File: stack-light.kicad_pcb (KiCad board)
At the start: 2 copper layers, 82 x 56.5 mm, 129 parts, among them J2 Mini-DIN-6, J3 Barrel_Jack_Switch, J4 USB_C_Receptacle_USB2.0, Q1 2N7002, Q2 2N7002, Q3 2N7002, Q4 2N7002, Q5 2N7002, Q6 BC817-40, Q7 BC817-40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

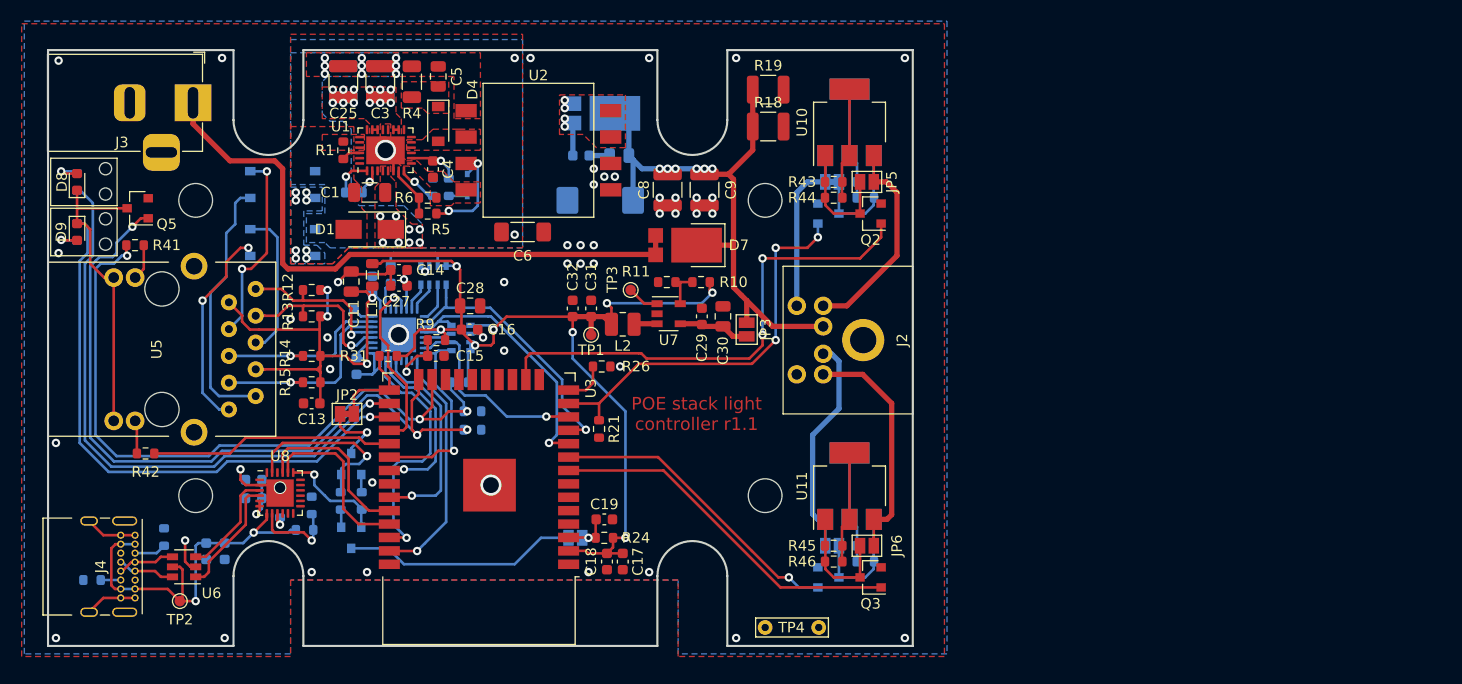
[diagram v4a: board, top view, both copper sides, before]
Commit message: Reduce case screw notch size and placement to better match case
Also center the mini-din output connector
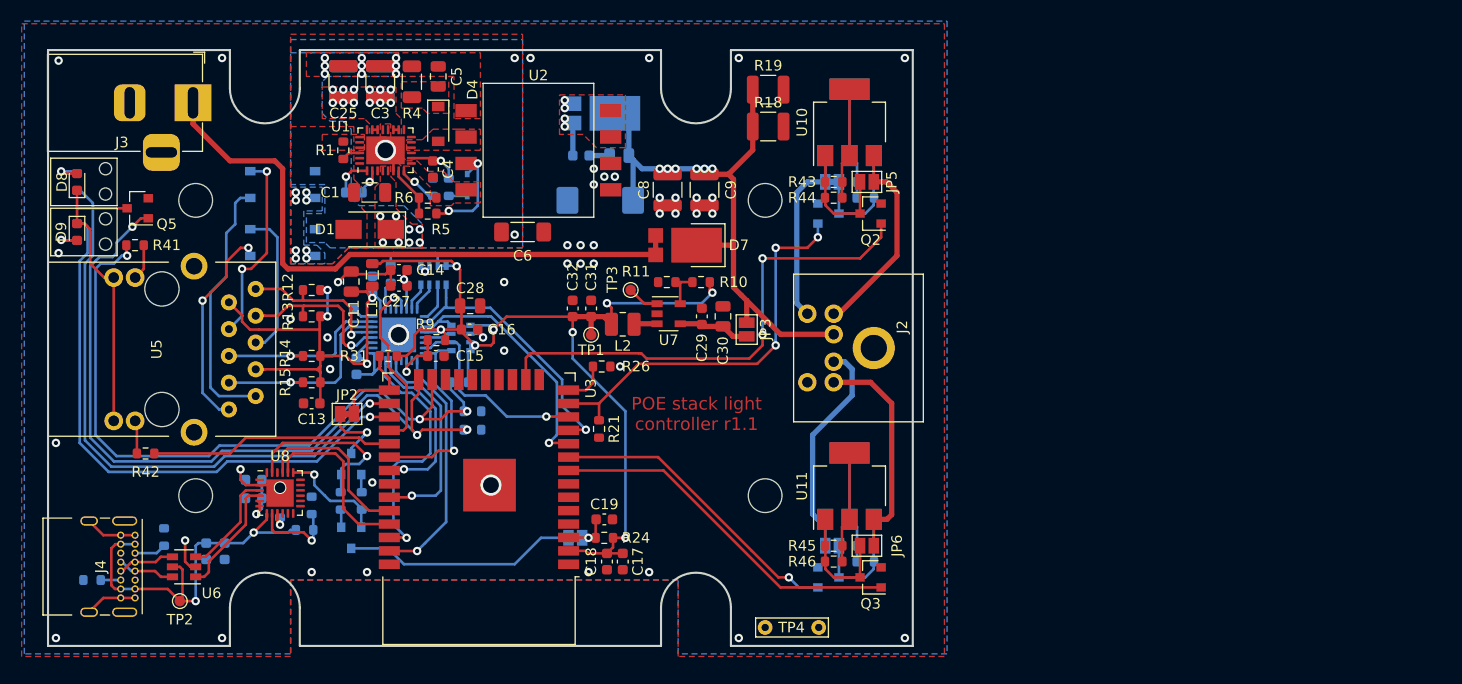
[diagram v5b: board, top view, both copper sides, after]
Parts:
- moved J2 1.25 mm to (183.0, 78.2)
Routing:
- net /Output/Drive_Green: track 22.6 -> 21.3 mm
- net +12V: track 57.1 -> 58.4 mm
- net /Output/Drive_Buzzer: track 16.4 -> 17.5 mm
- net /Output/Drive_Yellow: track 20.1 -> 19.4 mm
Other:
- outline, holes or cut-outs redrawn

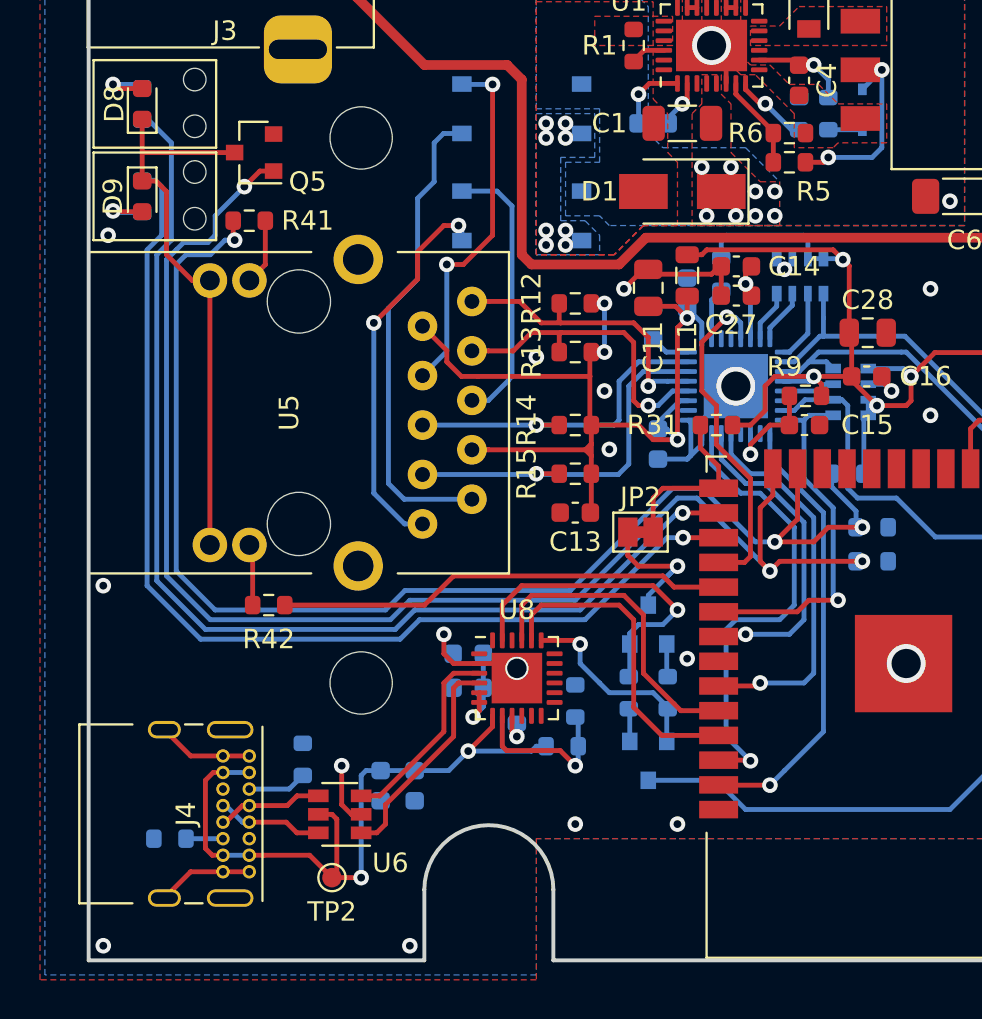
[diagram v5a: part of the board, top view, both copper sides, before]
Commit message: Adjust front IO to work with a flush panel
also removed the LED enable transistor
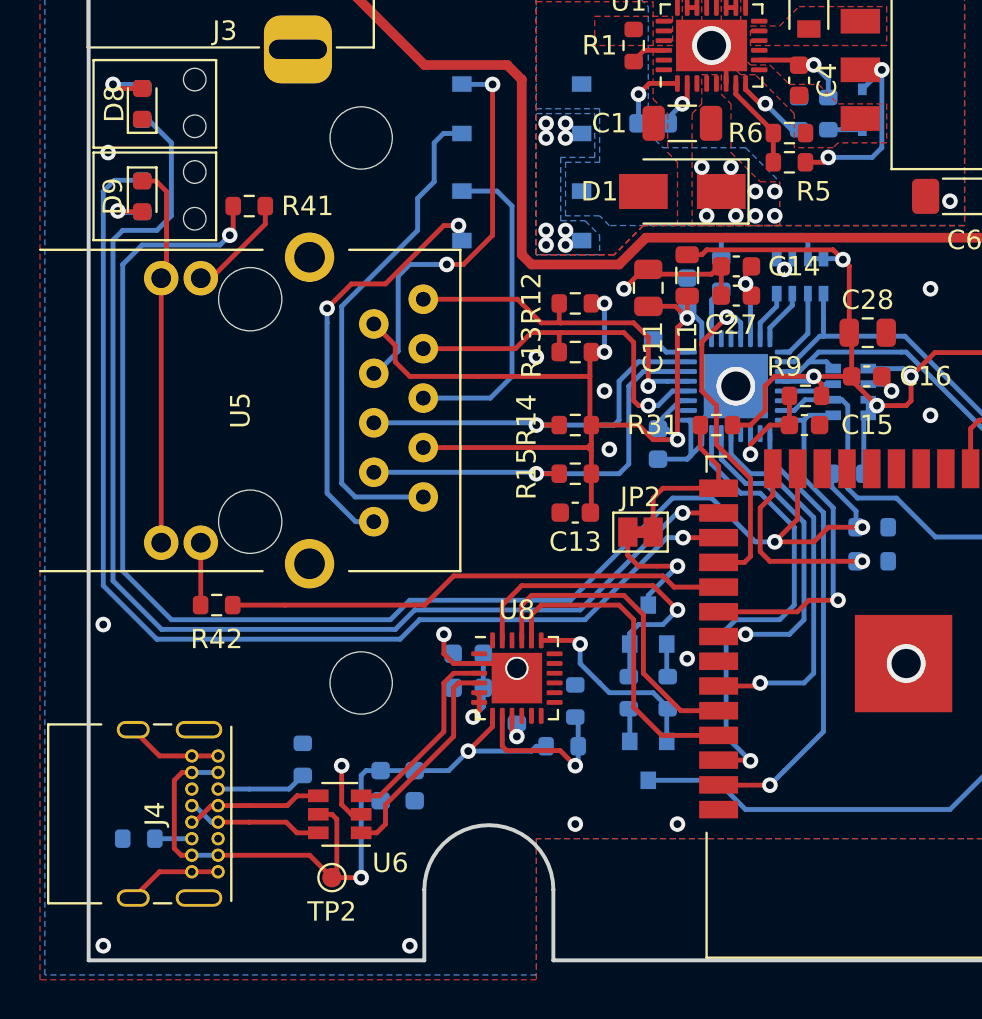
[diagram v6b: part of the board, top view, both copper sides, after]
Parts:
- removed Q5: 2N7002, Package_TO_SOT_SMD:SOT-23
- moved R42 2.67 mm to (106.6, 88.2)
- moved U5 2.50 mm to (108.3, 78.2)
- moved J4 1.60 mm to (106.7, 96.0)
- moved R39 1.60 mm to (102.6, 100.2)
- moved R41 0.75 mm to (108.2, 67.8)
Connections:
- net LED_EN renamed Net-(R25-Pad1)
- D8 pad 1: LED_GND -> GND
- D9 pad 1: LED_GND -> GND
- U5 pad 12: LED_GND -> GND
- U5 pad 14: LED_GND -> GND
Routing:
- net Net-(R25-Pad1): track 71.3 -> 10.3 mm, vias 3 -> 1
- net LED_GND: track 29.0 -> 0.00 mm
- net GND: track 37.2 -> 56.8 mm
- net LED_status: track 68.2 -> 74.1 mm
- net Net-(C11-Pad2): track 49.4 -> 54.4 mm
- net LED_LOCATE: track 57.2 -> 61.4 mm
- net LED_ARTNET: track 54.6 -> 57.4 mm
- net LED_net: track 23.1 -> 25.8 mm
- net /Ethernet Controller/TDP: track 15.5 -> 18.1 mm
- net /Ethernet Controller/RDP: track 17.4 -> 19.9 mm
- net /Ethernet Controller/RDN: track 19.4 -> 21.9 mm
- net /Ethernet Controller/TDN: track 16.2 -> 18.6 mm
- net POE_V2+: track 14.2 -> 16.7 mm
- net POE_V1+: track 18.5 -> 20.7 mm
- net Net-(R41-Pad1): track 3.46 -> 5.39 mm
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
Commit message: Add option for SIL regulator module due to component shortage
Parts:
- added U13: TSR_1-2433, Converter_DCDC:Converter_DCDC_TRACO_TSR-1_THT, F.Cu at (164.2, 80.8)
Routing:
- net +3V3: track 104.2 -> 113.6 mm
- net Yellow: track 47.0 -> 52.9 mm
- net Net-(C29-Pad1): track 6.80 -> 10.7 mm
- net Buzzer: track 38.5 -> 40.4 mm
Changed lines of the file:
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@@
     (thickness 1.6)
     (drawings 22)
-    (tracks 912)
+    (tracks 920)
     (zones 0)
-    (modules 128)
+    (modules 129)
     (nets 130)
   )
@@
     (add_net Yellow)
   )
+  (module Converter_DCDC:Converter_DCDC_TRACO_TSR-1_THT (layer F.Cu)
+    (at 164.25 80.75 180)
+    (descr "DCDC-Converter, TRACO, TSR 1-xxxx")
+    (tags "DCDC-Converter TRACO TSR-1")
+    (fp_text reference U13 (at -1.5 -6.71) (layer F.SilkS)
+      (effects (font (size 1 1) (thickness 0.15)))
+    )
+    (fp_text value TSR_1-2433 (at 2.5 3.25) (layer F.Fab)
+      (effects (font (size 1 1) (thickness 0.15)))
+    )
+    (fp_line (start -3.75 2.45) (end -1.42 2.45) (layer F.SilkS) (width 0.12))
+    (fp_line (start -3.75 0) (end -3.75 2.45) (layer F.SilkS) (width 0.12))
+    (fp_line (start -3.3 1) (end -2.3 2) (layer F.Fab) (width 0.1))
+    (fp_line (start -3.3 1) (end -3.3 -5.6) (layer F.Fab) (width 0.1))
+    (fp_line (start 8.4 2) (end 8.4 -5.6) (layer F.Fab) (width 0.1))
+    (fp_line (start -3.3 -5.6) (end 8.4 -5.6) (layer F.Fab) (width 0.1))
+    (fp_line (start -3.55 2.25) (end -3.55 -5.85) (layer F.CrtYd) (width 0.05))
+    (fp_line (start 8.65 2.25) (end -3.55 2.25) (layer F.CrtYd) (width 0.05))
+    (fp_line (start 8.65 -5.85) (end 8.65 2.25) (layer F.CrtYd) (width 0.05))
+    (fp_line (start -3.55 -5.85) (end 8.65 -5.85) (layer F.CrtYd) (width 0.05))
+    (fp_line (start 8.52 2.12) (end -3.42 2.12) (layer F.SilkS) (width 0.12))
+    (fp_line (start 8.52 -5.73) (end 8.52 2.12) (layer F.SilkS) (width 0.12))
+    (fp_line (start -3.42 -5.73) (end 8.52 -5.73) (layer F.SilkS) (width 0.12))
+    (fp_line (start -3.42 2.12) (end -3.42 -5.73) (layer F.SilkS) (width 0.12))
+    (fp_line (start -2.3 2) (end 8.4 2) (layer F.Fab) (width 0.1))
+    (fp_text user %R (at 3 -3) (layer F.Fab)
+      (effects (font (size 1 1) (thickness 0.15)))
+    )
+    (pad 3 thru_hole oval (at 5.08 0 180) (size 1.5 2.5) (drill 1) (layers *.Cu *.Mask)
+      (net 10 +3V3))
+    (pad 2 thru_hole oval (at 2.54 0 180) (size 1.5 2.5) (drill 1) (layers *.Cu *.Mask)
+      (net 6 GND))
+    (pad 1 thru_hole rect (at 0 0 180) (size 1.5 2.5) (drill 1) (layers *.Cu *.Mask)
+      (net 128 "Net-(C29-Pad1)"))
+    (model ${KISYS3DMOD}/Converter_DCDC.3dshapes/Converter_DCDC_TRACO_TSR-1_THT.wrl
+      (at (xyz 0 0 0))
+      (scale (xyz 1 1 1))
+      (rotate (xyz 0 0 0))
+    )
+  )
   (module TestPoint:TestPoint_Bridge_Pitch5.08mm_Drill0.7mm (layer F.Cu)
     (at 168 104.75)
@@
     )
   )
-  (gr_text "POE stack light\ncontroller r1.0" (at 161.5 84.5) (layer F.Mask)
+  (gr_text "POE stack light\ncontroller r1.0" (at 162.25 85.5) (layer F.Mask)
     (effects (font (size 1.2 1.2) (thickness 0.3)))
   )
-  (gr_text "POE stack light\ncontroller r1.1" (at 161.5 84.5) (layer F.Cu)
+  (gr_text "POE stack light\ncontroller r1.1" (at 162.25 85.5) (layer F.Cu)
     (effects (font (size 1.2 1.2) (thickness 0.3)))
   )
@@
   (segment (start 131.5 70.25) (end 131.75201 69.99799) (width 0.25) (layer F.Cu) (net 10))
   (segment (start 130.75 70.25) (end 131.5 70.25) (width 0.25) (layer F.Cu) (net 10))
+  (segment (start 159.17 80.75) (end 159.17 79.17) (width 0.5) (layer F.Cu) (net 10))
+  (segment (start 159.17 79.17) (end 158 78) (width 0.5) (layer F.Cu) (net 10))
+  (segment (start 158 78) (end 154 78) (width 0.5) (layer F.Cu) (net 10))
+  (segment (start 153.425 77.425) (end 153.425 76) (width 0.5) (layer F.Cu) (net 10))
+  (segment (start 154 78) (end 153.425 77.425) (width 0.5) (layer F.Cu) (net 10))
   (segment (start 114.65 76.46) (end 115.9 75.21) (width 0.25) (layer B.Cu) (net 11))
   (segment (start 118.4 70.75) (end 118.4 70.75) (width 0.25) (layer B.Cu) (net 11))
@@
   (segment (start 171.2 100.95) (end 170.25 100) (width 0.25) (layer B.Cu) (net 24))
   (segment (start 173 100.95) (end 171.2 100.95) (width 0.25) (layer B.Cu) (net 24))
-  (segment (start 145.75 78.75) (end 156 78.75) (width 0.25) (layer F.Cu) (net 25))
-  (segment (start 156.75 79.25) (end 166.5 79.25) (width 0.25) (layer F.Cu) (net 25))
-  (segment (start 145.31 79.19) (end 145.75 78.75) (width 0.25) (layer F.Cu) (net 25))
-  (segment (start 156 78.75) (end 156.25 78.75) (width 0.25) (layer F.Cu) (net 25))
-  (segment (start 156.25 78.75) (end 156.75 79.25) (width 0.25) (layer F.Cu) (net 25))
-  (segment (start 145.31 81.245) (end 145.31 79.19) (width 0.25) (layer F.Cu) (net 25))
-  (segment (start 167.75 78) (end 167.75 77) (width 0.25) (layer F.Cu) (net 25))
-  (segment (start 166.5 79.25) (end 167.75 78) (width 0.25) (layer F.Cu) (net 25))
   (via (at 167.75 77) (size 0.8) (drill 0.4) (layers F.Cu B.Cu) (net 25))
   (segment (start 167.75 77) (end 167.75 69.75) (width 0.25) (layer B.Cu) (net 25))
@@
   (segment (start 179 67.75) (end 179 66.45) (width 0.25) (layer F.Cu) (net 25))
   (segment (start 177 69.75) (end 179 67.75) (width 0.25) (layer F.Cu) (net 25))
+  (segment (start 145.75 78.75) (end 145.31 79.19) (width 0.25) (layer F.Cu) (net 25))
+  (segment (start 156.75 79.25) (end 156.25 78.75) (width 0.25) (layer F.Cu) (net 25))
+  (segment (start 156.75 81.5) (end 156.75 79.25) (width 0.25) (layer F.Cu) (net 25))
+  (segment (start 157.75 82.5) (end 156.75 81.5) (width 0.25) (layer F.Cu) (net 25))
+  (segment (start 145.31 79.19) (end 145.31 81.245) (width 0.25) (layer F.Cu) (net 25))
+  (segment (start 156.25 78.75) (end 145.75 78.75) (width 0.25) (layer F.Cu) (net 25))
+  (segment (start 166.5 82.5) (end 157.75 82.5) (width 0.25) (layer F.Cu) (net 25))
+  (segment (start 167.75 81.25) (end 166.5 82.5) (width 0.25) (layer F.Cu) (net 25))
+  (segment (start 167.75 77) (end 167.75 81.25) (width 0.25) (layer F.Cu) (net 25))
   (segment (start 158.365 89.865) (end 149.365 89.865) (width 0.25) (layer F.Cu) (net 26))
   (segment (start 169.45 100.95) (end 158.365 89.865) (width 0.25) (layer F.Cu) (net 26))
   (segment (start 179 100.95) (end 169.45 100.95) (width 0.25) (layer F.Cu) (net 26))
   (segment (start 149.365 83.515) (end 152.235 83.515) (width 0.25) (layer F.Cu) (net 27))
-  (via (at 169 78) (size 0.8) (drill 0.4) (layers F.Cu B.Cu) (net 27))
-  (segment (start 169 77.5) (end 169 68.75) (width 0.25) (layer B.Cu) (net 27))
+  (via (at 169 81.25) (size 0.8) (drill 0.4) (layers F.Cu B.Cu) (net 27))
   (via (at 169 68.75) (size 0.8) (drill 0.4) (layers F.Cu B.Cu) (net 27))
   (segment (start 169 68.75) (end 172 68.75) (width 0.25) (layer F.Cu) (net 27))
@@
   (segment (start 152.25 83.53) (end 152.235 83.515) (width 0.25) (layer F.Cu) (net 27))
   (segment (start 152.25 85.1) (end 152.25 83.53) (width 0.25) (layer F.Cu) (net 27))
-  (segment (start 169 77.5) (end 169 78) (width 0.25) (layer B.Cu) (net 27))
-  (segment (start 167.25 79.75) (end 169 78) (width 0.25) (layer F.Cu) (net 27))
-  (segment (start 156 79.75) (end 167.25 79.75) (width 0.25) (layer F.Cu) (net 27))
-  (segment (start 152.235 83.515) (end 156 79.75) (width 0.25) (layer F.Cu) (net 27))
+  (segment (start 152.78 83) (end 152.25 83.53) (width 0.25) (layer F.Cu) (net 27))
+  (segment (start 167.25 83) (end 152.78 83) (width 0.25) (layer F.Cu) (net 27))
+  (segment (start 169 81.25) (end 167.25 83) (width 0.25) (layer F.Cu) (net 27))
+  (segment (start 169 78) (end 169 81.25) (width 0.25) (layer B.Cu) (net 27))
+  (segment (start 169 68.75) (end 169 78) (width 0.25) (layer B.Cu) (net 27))
   (segment (start 176.7125 98.5) (end 176.7125 97) (width 0.25) (layer B.Cu) (net 28))
   (segment (start 176.7125 95.2125) (end 176 94.5) (width 0.25) (layer B.Cu) (net 28))
@@
   (segment (start 161.925 75.95) (end 162 76.025) (width 0.5) (layer F.Cu) (net 128))
   (segment (start 159.95 75.95) (end 161.925 75.95) (width 0.5) (layer F.Cu) (net 128))
+  (segment (start 164.25 77.85) (end 164.95 77.15) (width 0.5) (layer F.Cu) (net 128))
+  (segment (start 164.25 80.75) (end 164.25 77.85) (width 0.5) (layer F.Cu) (net 128))
   (segment (start 139.425 86) (end 139.5 86) (width 0.25) (layer B.Cu) (net 129))
   (via (at 139.75 86) (size 0.8) (drill 0.4) (layers F.Cu B.Cu) (net 129))

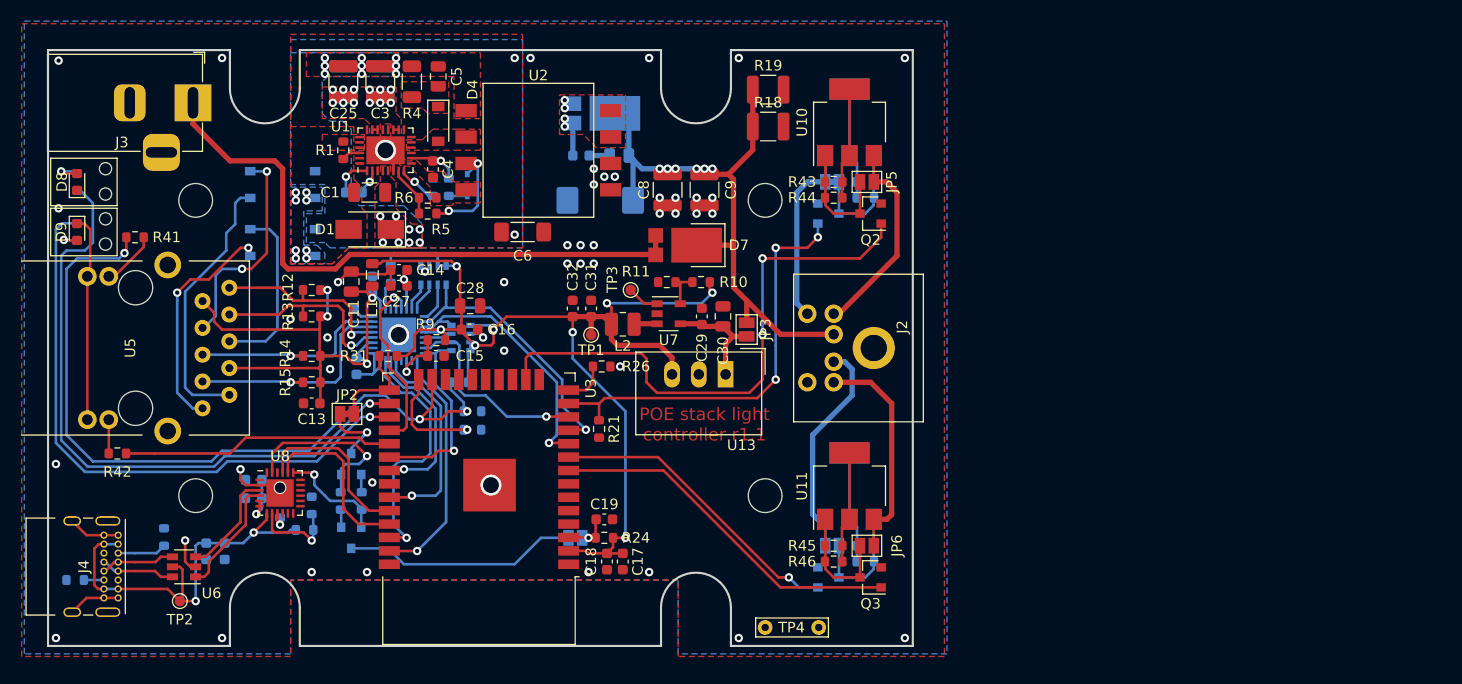
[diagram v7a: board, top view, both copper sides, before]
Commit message: Add PCB end panels
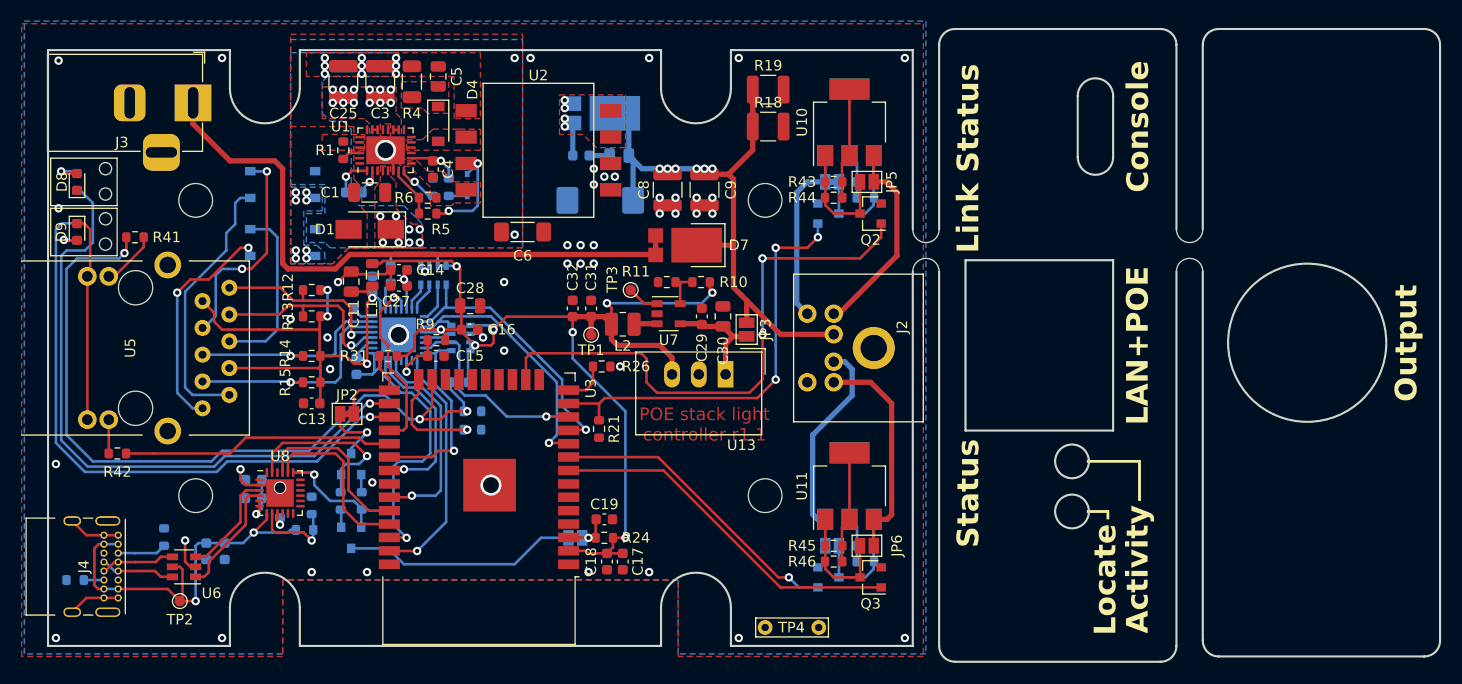
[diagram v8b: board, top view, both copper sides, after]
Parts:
- added svg2mod: G***, stack-light:panel_rear, F.Cu at (220.8, 77.8)
- added svg2mod: G***, stack-light:panel_front, F.Cu at (195.8, 78.0)
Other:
- board size 82 x 56.5 mm -> 132 x 60 mm
